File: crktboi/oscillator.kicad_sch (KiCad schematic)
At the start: 10 parts, among them Q1 BC847, Q2 BC847, Q3 2N7002, U1 GSC1102YB-3V4000

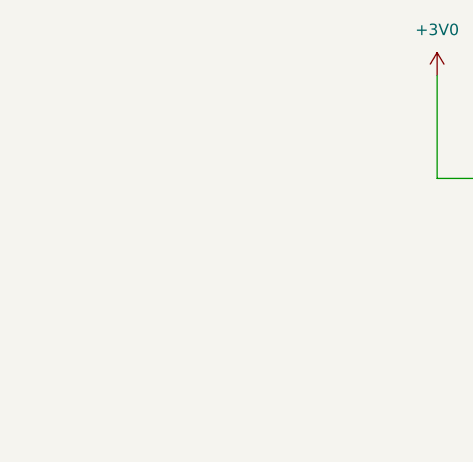
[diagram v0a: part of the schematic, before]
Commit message: Added the power circuit to the design and considered VBAT_OK as the power control output for the design. Still todo is reducing capacitor bank size and adjusting BQ25505 parameters
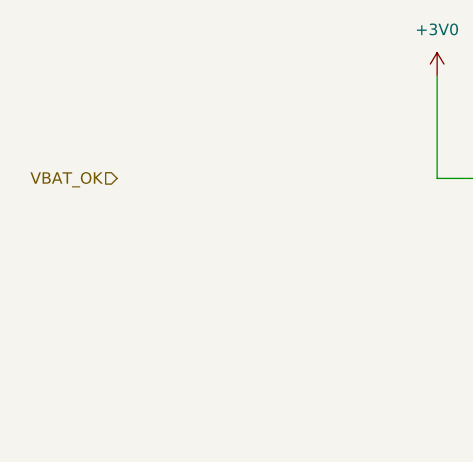
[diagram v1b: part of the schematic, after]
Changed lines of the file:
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@@
+		)
+	)
+	(hierarchical_label "VBAT_OK"
+		(shape input)
+		(at 27.94 62.23 180)
+		(effects
+			(font
+				(size 1.27 1.27)
+			)
+			(justify right)
 		)
 	)
